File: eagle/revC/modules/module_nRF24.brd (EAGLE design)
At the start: 24.1 x 32.8 mm, 10 parts

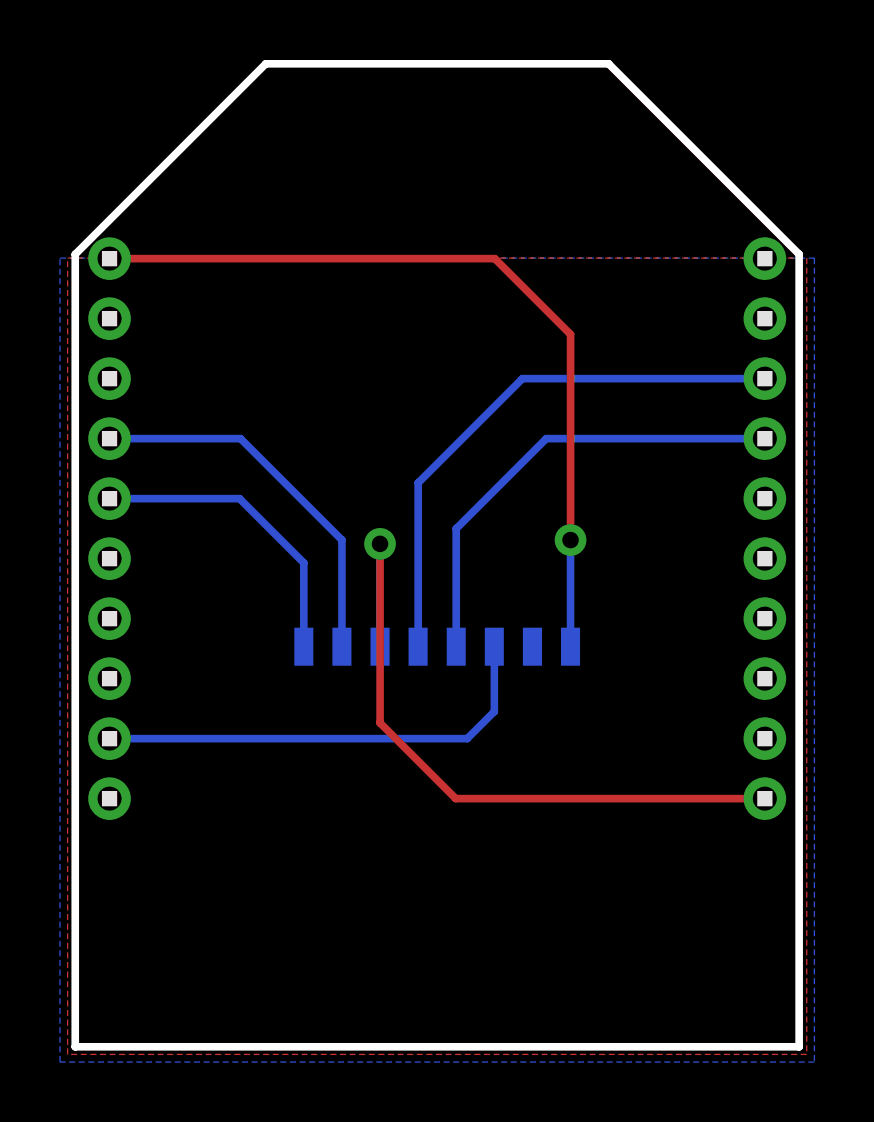
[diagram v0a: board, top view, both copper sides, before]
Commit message: Replaced modules with library parts
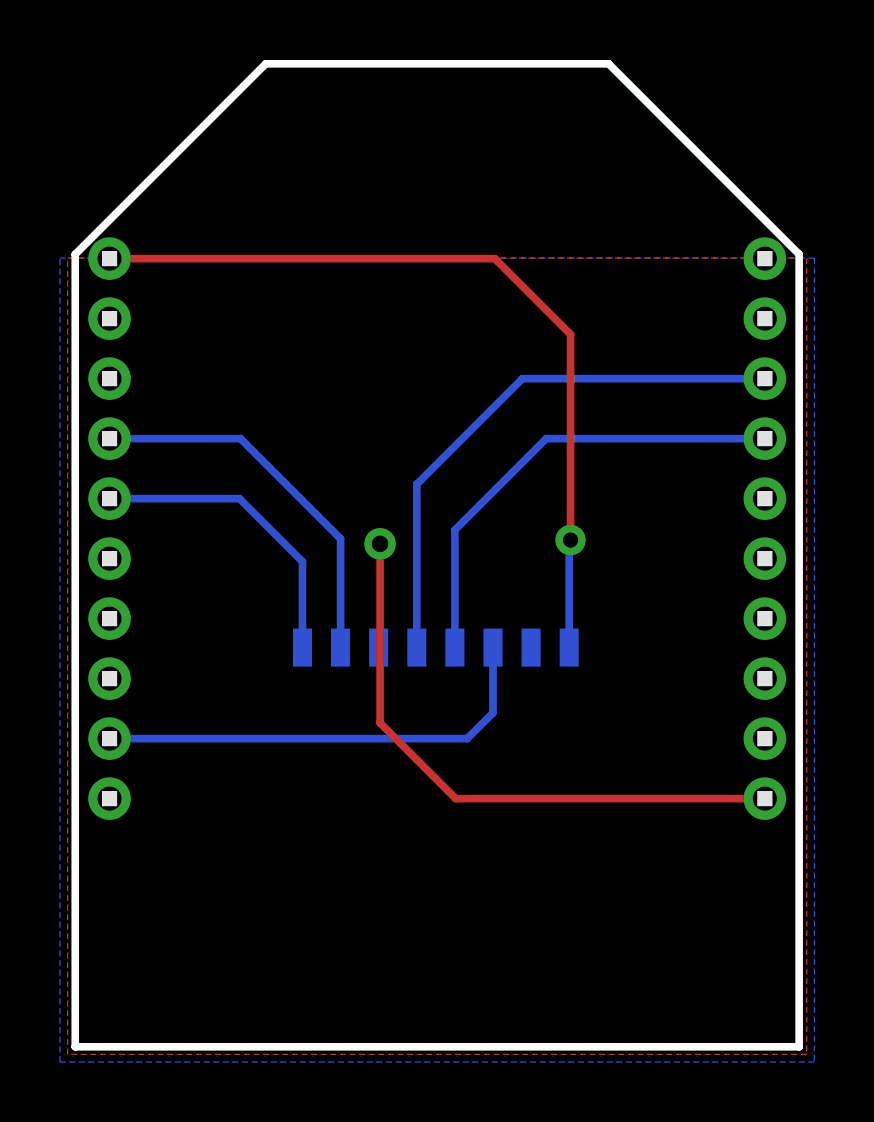
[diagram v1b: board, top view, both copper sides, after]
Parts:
- removed 3.3V, CE, CSN, GND, IRQ, MISO, MOSI, SCK: (no value), wirepad:SMD0,65-1,27
- added U$1: NRF24, RadioShield:NRF24
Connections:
- net GND: now also U$1.GND; no longer GND.1
- net INT0: now also U$1.CE; no longer CE.1
- net INT1: now also U$1.IRQ; no longer IRQ.1
- net SPI_CS: now also U$1.CS; no longer CSN.1
- net SPI_MISO: now also U$1.MISO; no longer MISO.1
- net SPI_MOSI: now also U$1.MOSI; no longer MOSI.1
- net SPI_SCK: now also U$1.SCK; no longer SCK.1
- net VCC: now also U$1.3.3V; no longer 3.3V.1
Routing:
- net SPI_MOSI: track 23.3 -> 19.8 mm
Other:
- board text removed: "3.3V"
- board text removed: "CE"
- board text removed: "CSN"
- board text removed: "GND"
- board text removed: "IRQ"
- board text removed: "MISO"
- board text removed: "MOSI"
- board text removed: "SCK"

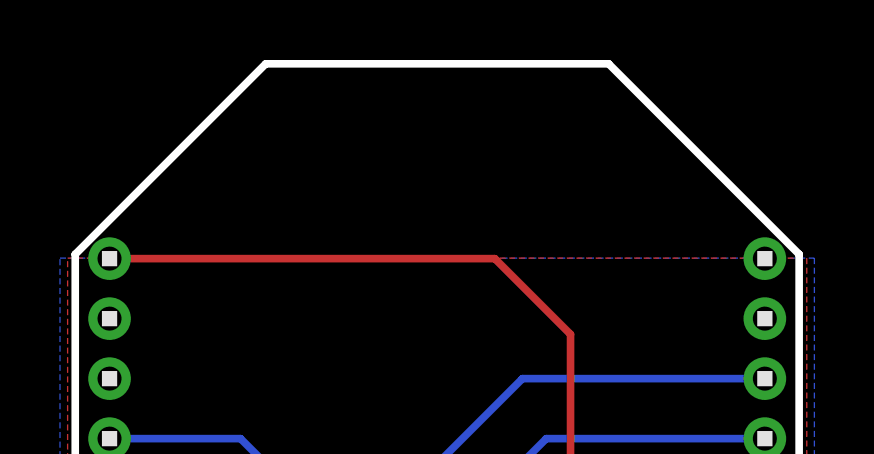
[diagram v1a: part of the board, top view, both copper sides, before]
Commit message: Fixed module name layers
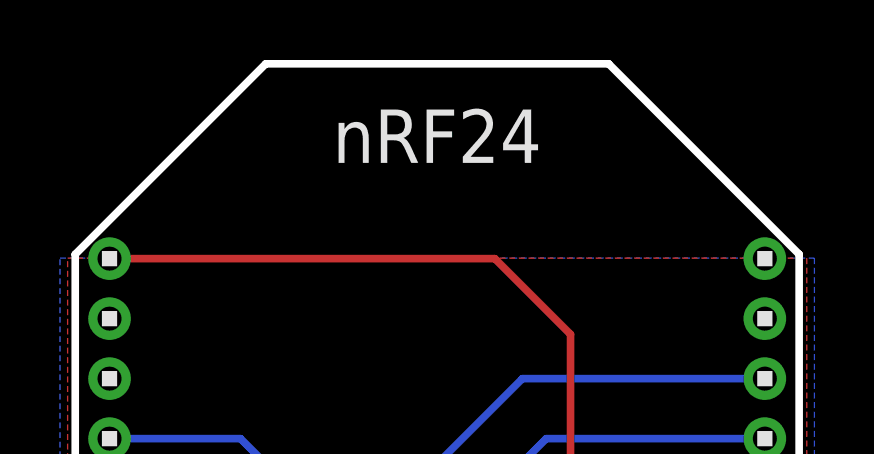
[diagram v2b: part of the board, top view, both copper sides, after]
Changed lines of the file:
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@@
 <wire x1="24.257" y1="26.543" x2="24.257" y2="0.127" width="0.254" layer="20"/>
 <wire x1="24.257" y1="0.127" x2="0.127" y2="0.127" width="0.254" layer="20"/>
-<text x="12.192" y="30.48" size="1.778" layer="51" ratio="15" rot="SR0" align="center">nRF24</text>
+<text x="12.192" y="30.48" size="1.778" layer="25" ratio="15" rot="SR0" align="center">nRF24</text>
 </plain>
 <attributes>
